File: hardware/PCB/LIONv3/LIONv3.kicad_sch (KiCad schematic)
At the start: 54 parts, among them J1 Conn_01x14, U1 TPS259474ARPWR, U14 E80-900M2213S, U2 ESP32-C6-MINI-1-N4, U3 TPS259472ARPWR, U4 TLV75533PDQNR, U5 TCAN3414DR, U6 TMP112AIDRLR, U7 INA226AIDGSR, U9 INA226AIDGSR

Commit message: feat(hardware): organize schematic pages
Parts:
- removed C1, C2: 1uF, Capacitor_SMD:C_0603_1608Metric, symbol Device:C_Small
- removed C10, C22, C23, C9: 100nF, Capacitor_SMD:C_0402_1005Metric, symbol Device:C_Small
- removed C21: 22uF, Capacitor_SMD:C_0805_2012Metric, symbol Device:C_Small
- removed C3: 3.3nF, Capacitor_SMD:C_0402_1005Metric, symbol Device:C_Small
- removed C4: 2.2nF, Capacitor_SMD:C_0402_1005Metric, symbol Device:C_Small
- removed C5, C7: 1uF, Capacitor_SMD:C_0402_1005Metric, symbol Device:C_Small
- removed D1, D2, D3, D4: LED, Capacitor_SMD:C_0402_1005Metric, symbol Device:LED
- removed D5, D6: D_Schottky, Diode_SMD:D_0402_1005Metric, symbol Device:D_Schottky
- removed R1, R2, R3, R4: 1k, Resistor_SMD:R_0402_1005Metric, symbol Device:R_Small
- removed R10, R15, R28, R45, R6: 10k, Resistor_SMD:R_0402_1005Metric, symbol Device:R_Small
- removed R11, R16: 2m, TET-Footprints:RES-SMD_L6.3-W3.1-1, symbol Device:R_Small
- removed R5: 133k, Resistor_SMD:R_0402_1005Metric, symbol Device:R_Small
- removed R7: 100k, Resistor_SMD:R_0402_1005Metric, symbol Device:R_Small
- removed R8: 6.65k, Resistor_SMD:R_0402_1005Metric, symbol Device:R_Small
- removed R9: 15k, Resistor_SMD:R_0402_1005Metric, symbol Device:R_Small
- removed U1: TPS259474ARPWR, LIONv3-Footprints:VQFN-10_L2.0-W2.0-P0.45-TL, symbol LIONv3-Symbols:TPS259474ARPWR
- removed U14: E80-900M2213S, LIONv3-Footprints:WIFIM-SMD_22P-L26.0-W16.0-P1.27-TL, symbol TET-Symbols:E80-900M2213S_C42464134
- removed U3: TPS259472ARPWR, LIONv3-Footprints:VQFN-10_L2.0-W2.0-P0.45-TL, symbol LIONv3-Symbols:TPS259472ARPWR
- removed U4: TLV75533PDQNR, LIONv3-Footprints:X2SON-4_L1.0-W1.0-P0.65-TL-EP, symbol LIONv3-Symbols:TLV75533PDQNR
- removed U7, U9: INA226AIDGSR, LIONv3-Footprints:MSOP-10_L3.0-W3.0-P0.50-LS5.0-BL, symbol TET-Symbols:INA226AIDGSR
- R12, R13: value 60.4 -> 61
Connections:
- no-connect marks 1 -> 0
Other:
- added sheet POWER (POWER.kicad_sch)
- added sheet RF (RF.kicad_sch)
- note removed: "LORA TRANSCEIVER"
- note removed: "POWER CURRENT MONITOR"
- moved on the sheet: C14, C29, C6, C8, H1, H2, H3, H4, J1, JP2, R12, R13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

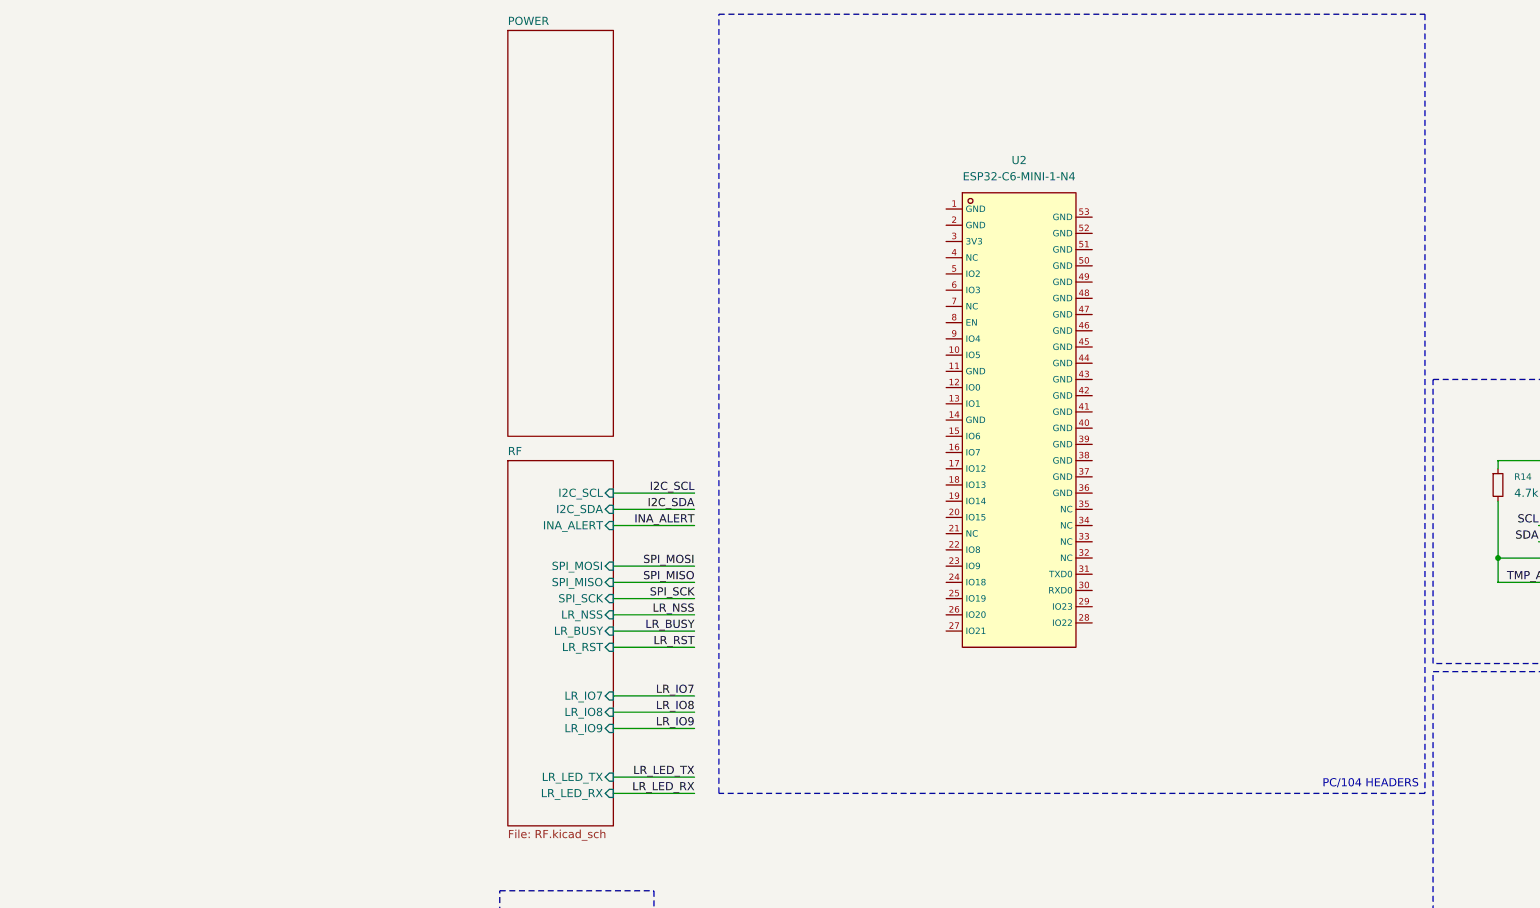
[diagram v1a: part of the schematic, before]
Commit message: feat(hardware): add ESP32-C6 UART0
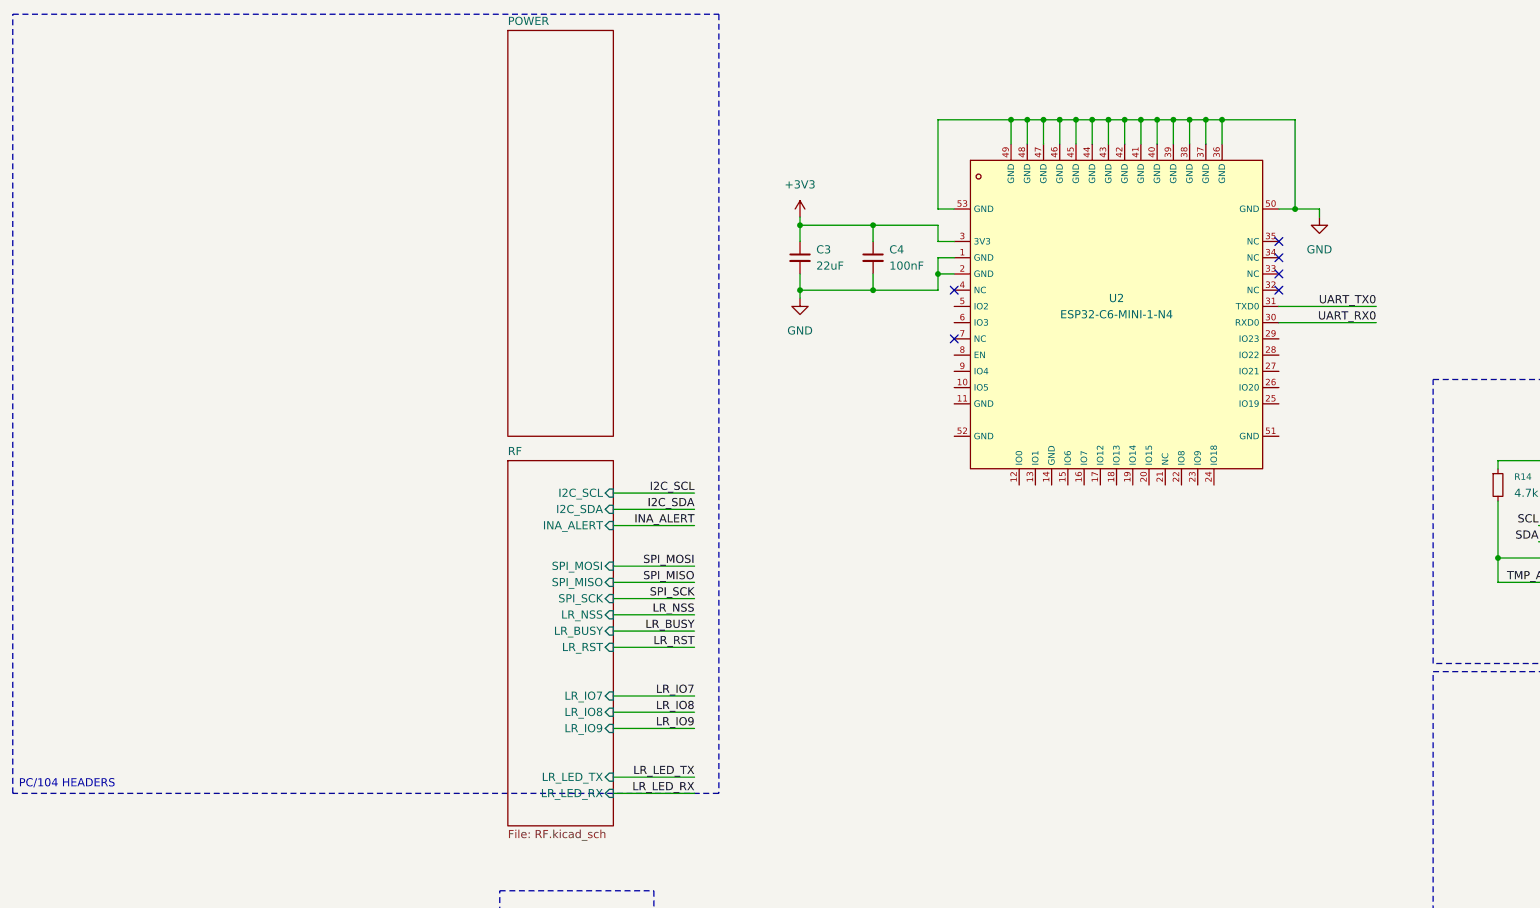
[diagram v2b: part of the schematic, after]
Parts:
- added C3: 22uF, symbol Device:C_Small
- added C4: 100nF, symbol Device:C_Small
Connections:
- net GND: now also U2.1 (GND), U2.2 (GND), U2.36 (GND), U2.37 (GND), U2.38 (GND), U2.39 (GND), U2.40 (GND), U2.41 (GND), U2.42 (GND), U2.43 (GND), U2.44 (GND), U2.45 (GND), U2.46 (GND), U2.47 (GND), U2.48 (GND), U2.49 (GND), U2.50 (GND), U2.53 (GND), C3.2, C4.2
- net +3V3: now reaches U2.3 (3V3)
- net +3V3: now also C3.1, C4.1
- net UART_RX0: now reaches U2.30 (RXD0)
- net UART_TX0: now reaches U2.31 (TXD0)
- no-connect marks 0 -> 6
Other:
- moved on the sheet: U2

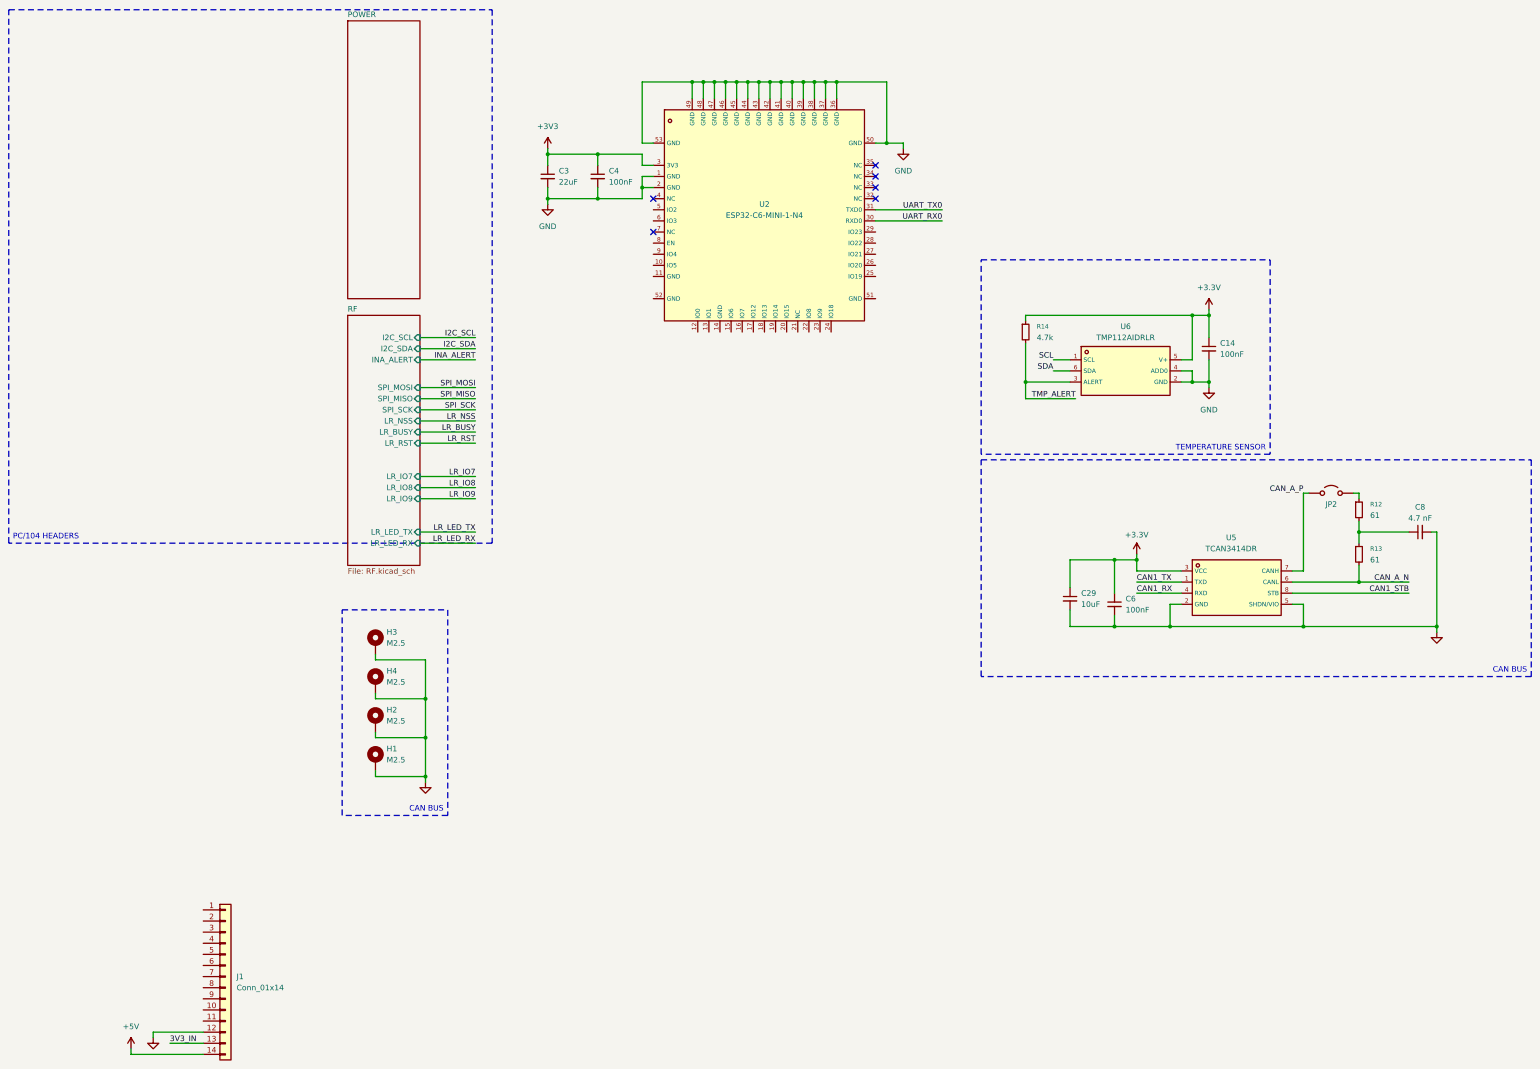
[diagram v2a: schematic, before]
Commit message: feat(hardware): finish ESP32-C6 electrical schematic
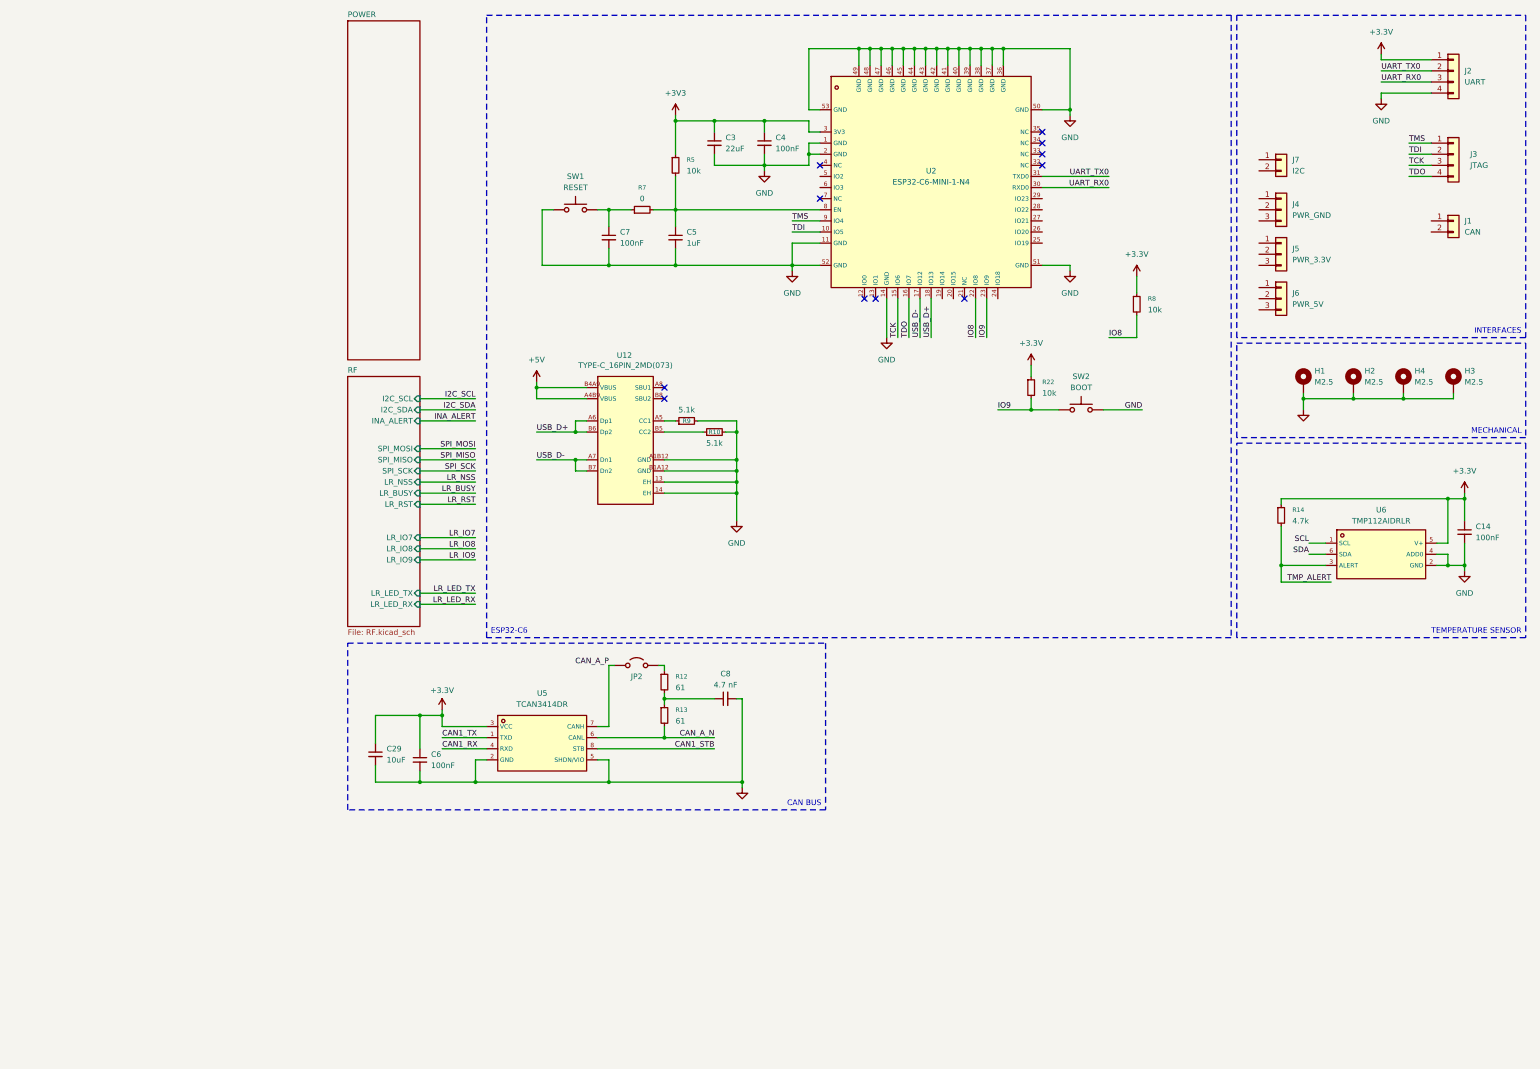
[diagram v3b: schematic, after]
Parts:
- removed J1: Conn_01x14, Connector_PinHeader_2.54mm:PinHeader_1x14_P2.54mm_Vertical_SMD_Pin1Left, symbol Connector_Generic:Conn_01x14
- added C5: 1uF, Capacitor_SMD:C_0603_1608Metric, symbol Device:C_Small
- added C7: 100nF, Capacitor_SMD:C_0402_1005Metric, symbol Device:C_Small
- added J1: CAN, Connector_Molex:Molex_PicoBlade_53048-0210_1x02_P1.25mm_Horizontal, symbol Connector_Generic:Conn_01x02
- added J2: UART, Connector_Molex:Molex_PicoBlade_53048-0410_1x04_P1.25mm_Horizontal, symbol Connector_Generic:Conn_01x04
- added J3: JTAG, Connector_Molex:Molex_PicoBlade_53048-0410_1x04_P1.25mm_Horizontal, symbol Connector_Generic:Conn_01x04
- added J4: PWR_GND, Connector_Molex:Molex_PicoBlade_53048-0310_1x03_P1.25mm_Horizontal, symbol Connector_Generic:Conn_01x03
- added J5: PWR_3.3V, Connector_Molex:Molex_PicoBlade_53048-0310_1x03_P1.25mm_Horizontal, symbol Connector_Generic:Conn_01x03
- added J6: PWR_5V, Connector_Molex:Molex_PicoBlade_53048-0310_1x03_P1.25mm_Horizontal, symbol Connector_Generic:Conn_01x03
- added J7: I2C, Connector_Molex:Molex_PicoBlade_53048-0210_1x02_P1.25mm_Horizontal, symbol Connector_Generic:Conn_01x02
- added R10, R9: 5.1k, Resistor_SMD:R_0402_1005Metric, symbol Device:R_Small
- added R22: 10k, symbol Device:R_Small
- added R5, R8: 10k, Resistor_SMD:R_0402_1005Metric, symbol Device:R_Small
- added R7: 0, Resistor_SMD:R_0402_1005Metric, symbol Device:R_Small
- added SW1: RESET, symbol Switch:SW_Push
- added SW2: BOOT, symbol Switch:SW_Push
- added U12: TYPE-C_16PIN_2MD(073), LIONv3-Footprints:USB-C-SMD_TYPE-C-16PIN-2MD-073, symbol LIONv3-Symbols:TYPE-C_16PIN_2MD(073)
- C3: footprint (none) -> Capacitor_SMD:C_0805_2012Metric
- C4: footprint (none) -> Capacitor_SMD:C_0402_1005Metric
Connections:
- net +3.3V: now also J2.1 (Pin_1), R22.1, R8.1
- net +3V3: now also R5.1
- net +5V: now also U12.A4B9 (VBUS), U12.B4A9 (VBUS)
- net GND: now also U2.11 (GND), U2.14 (GND), U2.51 (GND), U2.52 (GND), C5.2, C7.2, J2.4 (Pin_4), R10.2, R9.2, SW1.1, SW2.2, U12.13 (EH), U12.14 (EH), U12.A1B12 (GND), U12.B1A12 (GND)
- net UART_RX0: now also J2.3 (Pin_3)
- net UART_TX0: now also J2.2 (Pin_2)
- net TDI: now reaches U2.10 (IO5)
- net TDI: now also J3.2 (Pin_2)
- net TCK: now reaches U2.15 (IO6)
- net TCK: now also J3.3 (Pin_3)
- net TDO: now reaches U2.16 (IO7)
- net TDO: now also J3.4 (Pin_4)
- net USB_D-: now reaches U2.17 (IO12)
- net USB_D-: now also U12.A7 (Dn1), U12.B7 (Dn2)
- net USB_D+: now reaches U2.18 (IO13)
- net USB_D+: now also U12.A6 (Dp1), U12.B6 (Dp2)
- net IO8: now reaches U2.22 (IO8)
- net IO8: now also R8.2
- net IO9: now reaches U2.23 (IO9)
- net IO9: now also R22.2, SW2.1
- net at U2.8 (EN): now also C5.1, R5.2, R7.2
- net TMS: now reaches U2.9 (IO4)
- net TMS: now also J3.1 (Pin_1)
- new net: R10.1, U12.B5 (CC2)
- new net: C7.1, R7.1, SW1.2
- new net: R9.1, U12.A5 (CC1)
- no-connect marks 6 -> 11
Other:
- title: (none) -> LIONv3
- moved on the sheet: C14, C29, C3, C4, C6, C8, H1, H2, H3, H4, JP2, R12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
